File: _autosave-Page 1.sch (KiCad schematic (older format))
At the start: 35 parts, among them J1 10118192-0001LF, J2 ARJM11A3, U1 AZ1117-3.3, U2 LAN8720A

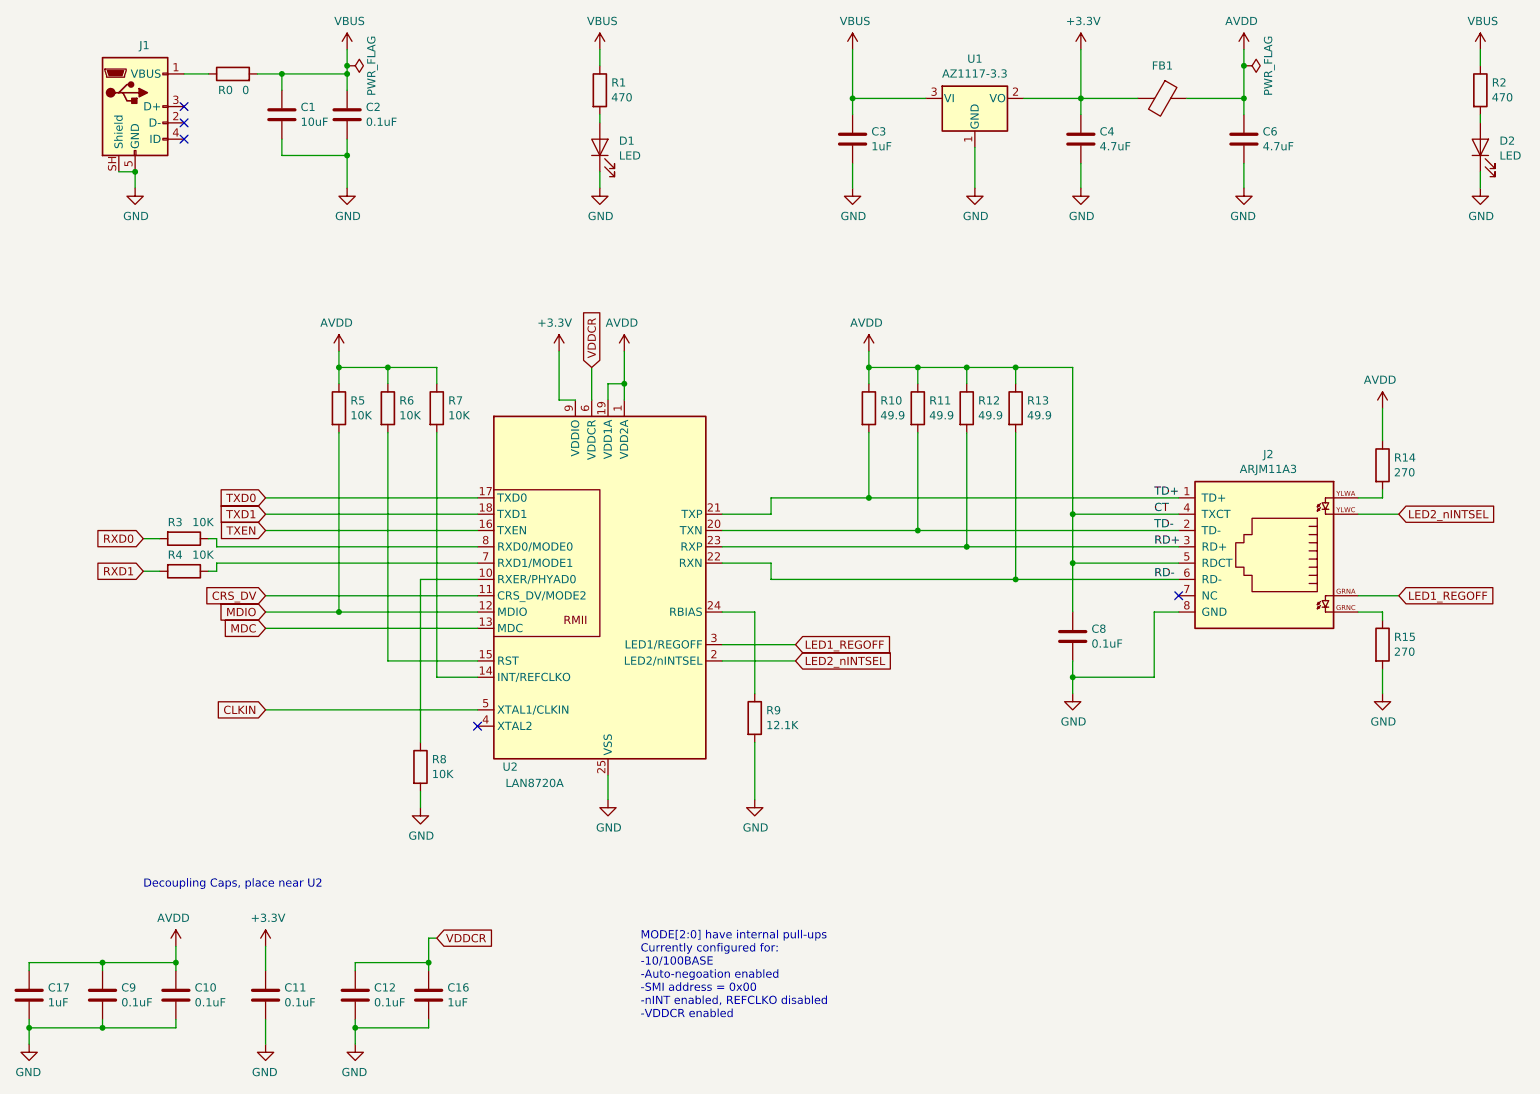
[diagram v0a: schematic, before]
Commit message: Started laying out board
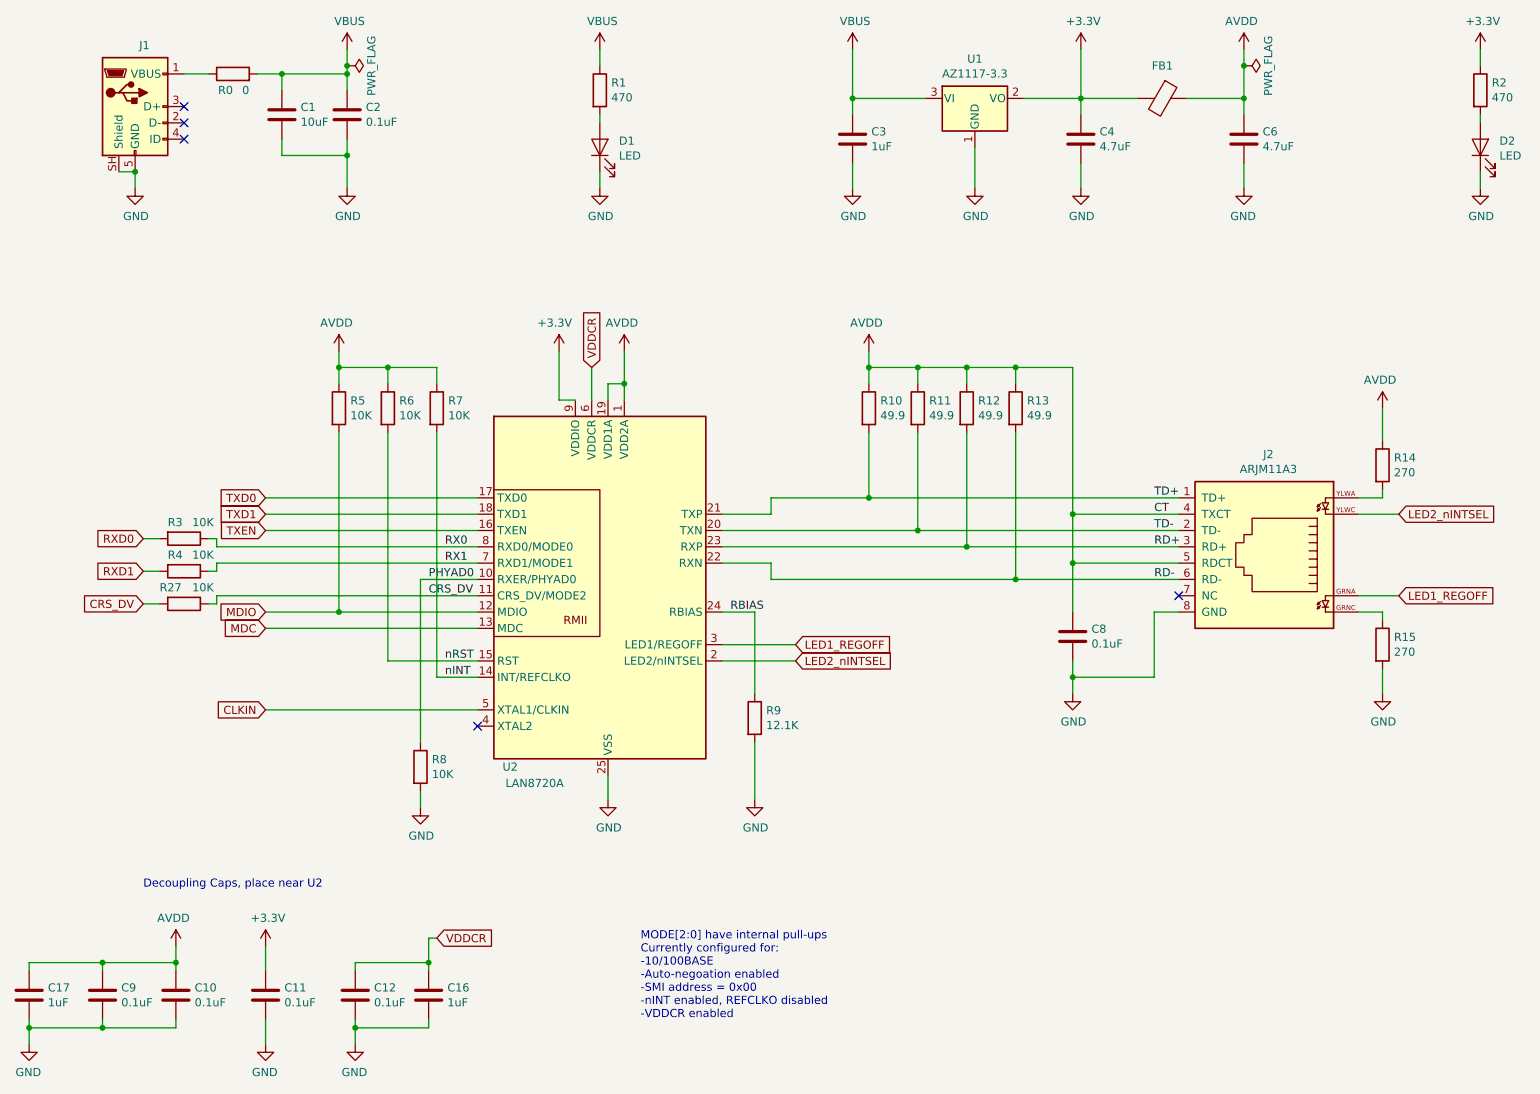
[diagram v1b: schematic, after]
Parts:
- added R27: 10K, Resistor_SMD:R_0603_1608Metric, symbol Device:R
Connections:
- net +3V3: now also R2.1
- net CRS_DV: now also R27.1, R27.2
- net VBUS: no longer R2.1
- net PHYAD0: now reaches R8.1, U2.10 (RXER/PHYAD0)
- net nINT: now reaches R7.2, U2.14 (INT/REFCLKO)
- net nRST: now reaches R6.2, U2.15 (RST)
- net RBIAS: now reaches R9.1, U2.24 (RBIAS)
- net RX1: now reaches R4.1, U2.7 (RXD1/MODE1)
- net RX0: now reaches R3.1, U2.8 (RXD0/MODE0)
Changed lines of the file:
@@
 	6150 1950 6150 2100
-$Comp
-L power:VBUS #PWR?
-U 1 1 5DF04C3D
-P 10000 1250
-AR Path="/5DF04C3D" Ref="#PWR?"  Part="1"
-AR Path="/5DED2F9B/5DF04C3D" Ref="#PWR0111"  Part="1"
-F 0 "#PWR0111" H 10000 1100 50  0001 C CNN
-F 1 "VBUS" H 10015 1423 50  0000 C CNN
-F 2 "" H 10000 1250 50  0001 C CNN
-F 3 "" H 10000 1250 50  0001 C CNN
-	1    10000 1250
-	1    0    0    -1
-$EndComp
 $Comp
 L power:GND #PWR?
@@
 Text GLabel 2550 4700 0    50   Input ~ 0
 MDIO
-Text GLabel 2550 4600 0    50   Input ~ 0
+Text GLabel 1800 4650 0    50   Input ~ 0
 CRS_DV
 Text GLabel 1800 4450 0    50   Input ~ 0
@@
 	2550 4200 3850 4200
 Wire Wire Line
-	3850 4600 2550 4600
-Wire Wire Line
 	3000 4700 2550 4700
 Connection ~ 3000 4700
@@
 Wire Wire Line
 	8550 1950 8550 2100
+Wire Wire Line
+	1800 4650 1900 4650
+Wire Wire Line
+	2200 4650 2250 4650
+Wire Wire Line
+	2250 4650 2250 4600
+Wire Wire Line
+	2250 4600 3850 4600
+$Comp
+L Device:R R?
+U 1 1 5DFF908E
+P 2050 4650
+AR Path="/5DFF908E" Ref="R?"  Part="1"
+AR Path="/5DED2F9B/5DFF908E" Ref="R27"  Part="1"
+F 0 "R27" V 1950 4500 50  0000 L CNN
+F 1 "10K" V 1950 4700 50  0000 L CNN
+F 2 "Resistor_SMD:R_0603_1608Metric" V 1980 4650 50  0001 C CNN
+F 3 "~" H 2050 4650 50  0001 C CNN
+	1    2050 4650
+	0    1    1    0
+$EndComp
+Text Label 3650 5000 0    50   ~ 0
+nRST
+Text Label 3650 5100 0    50   ~ 0
+nINT
+Text Label 3550 4500 0    50   ~ 0
+PHYAD0
+Text Label 5400 4700 0    50   ~ 0
+RBIAS
+Text Label 3650 4300 0    50   ~ 0
+RX0
+Text Label 3650 4400 0    50   ~ 0
+RX1
+Text Label 3550 4600 0    50   ~ 0
+CRS_DV
+$Comp
+L power:+3.3V #PWR?
+U 1 1 5E17203C
+P 10000 1250
+AR Path="/5E17203C" Ref="#PWR?"  Part="1"
+AR Path="/5DED2F9B/5E17203C" Ref="#PWR0111"  Part="1"
+F 0 "#PWR0111" H 10000 1100 50  0001 C CNN
+F 1 "+3.3V" H 10015 1423 50  0000 C CNN
+F 2 "" H 10000 1250 50  0001 C CNN
+F 3 "" H 10000 1250 50  0001 C CNN
+	1    10000 1250
+	1    0    0    -1
+$EndComp
 $EndSCHEMATC
